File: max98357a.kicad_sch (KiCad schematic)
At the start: 12 parts, among them U6 MAX98357A

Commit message: ESP32S3 push before GPIO label changes
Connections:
- net pad renamed PAD
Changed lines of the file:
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@@
 		)
 	)
-	(hierarchical_label "pad"
+	(hierarchical_label "PAD"
 		(shape input)
 		(at 147.32 116.84 270)

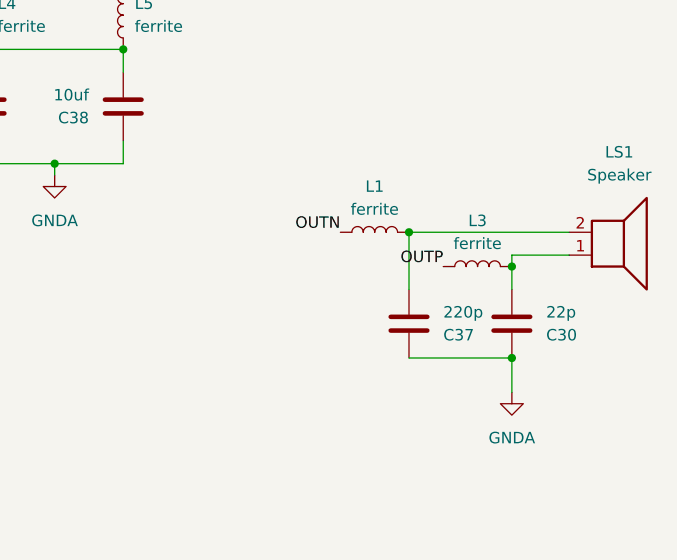
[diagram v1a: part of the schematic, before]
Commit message: ESP32S3: rename hierarchical GPIO labels and remove PCB tracks
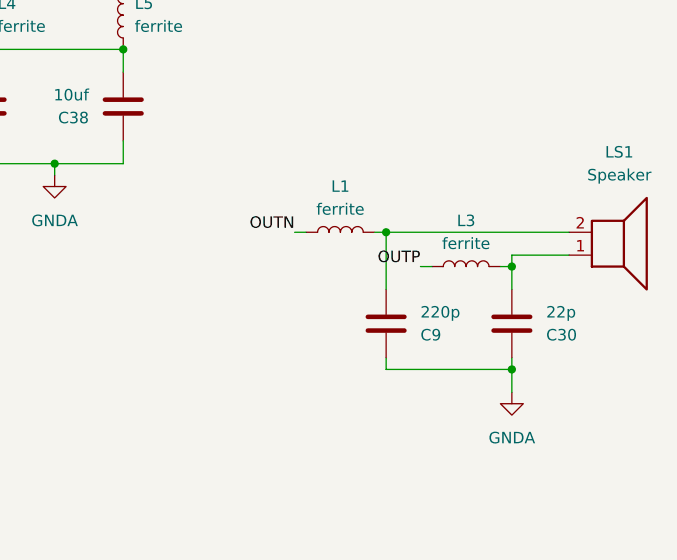
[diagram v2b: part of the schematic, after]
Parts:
- LS1: footprint (none) -> Connector_Molex:Molex_Micro-Latch_53253-0270_1x02_P2.00mm_Vertical
- renumbered C37 to C9
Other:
- moved on the sheet: C9, L1, L3
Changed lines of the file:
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@@
 	)
 	(junction
-		(at 220.98 106.68)
+		(at 232.41 110.49)
 		(diameter 0)
 		(color 0 0 0 0)
 	)
 	(junction
-		(at 232.41 120.65)
+		(at 218.44 106.68)
 		(diameter 0)
 		(color 0 0 0 0)
@@
 	)
 	(junction
-		(at 232.41 110.49)
+		(at 232.41 121.92)
 		(diameter 0)
 		(color 0 0 0 0)
@@
 	(wire
 		(pts
-			(xy 232.41 120.65) (xy 220.98 120.65)
+			(xy 232.41 121.92) (xy 218.44 121.92)
+		)
+		(stroke
+			(width 0)
+			(type default)
+		)
+	)
+	(wire
+		(pts
+			(xy 218.44 106.68) (xy 218.44 113.03)
 		)
 		(stroke
@@
 	(wire
 		(pts
-			(xy 220.98 106.68) (xy 220.98 113.03)
-		)
-		(stroke
-			(width 0)
-			(type default)
-		)
-	)
-	(wire
-		(pts
 			(xy 173.99 96.52) (xy 173.99 99.06)
 		)
@@
 	(wire
 		(pts
+			(xy 208.28 106.68) (xy 209.55 106.68)
+		)
+		(stroke
+			(width 0)
+			(type default)
+		)
+	)
+	(wire
+		(pts
 			(xy 173.99 86.36) (xy 189.23 86.36)
 		)
@@
 	(wire
 		(pts
+			(xy 231.14 110.49) (xy 232.41 110.49)
+		)
+		(stroke
+			(width 0)
+			(type default)
+		)
+	)
+	(wire
+		(pts
 			(xy 173.99 99.06) (xy 181.61 99.06)
 		)
@@
 	(wire
 		(pts
+			(xy 218.44 106.68) (xy 238.76 106.68)
+		)
+		(stroke
+			(width 0)
+			(type default)
+		)
+	)
+	(wire
+		(pts
 			(xy 121.92 120.65) (xy 121.92 116.84)
 		)
@@
 	(wire
 		(pts
+			(xy 232.41 121.92) (xy 232.41 124.46)
+		)
+		(stroke
+			(width 0)
+			(type default)
+		)
+	)
+	(wire
+		(pts
 			(xy 189.23 99.06) (xy 181.61 99.06)
 		)
@@
 	(wire
 		(pts
+			(xy 218.44 121.92) (xy 218.44 120.65)
+		)
+		(stroke
+			(width 0)
+			(type default)
+		)
+	)
+	(wire
+		(pts
 			(xy 83.82 139.7) (xy 74.93 139.7)
 		)
@@
 	(wire
 		(pts
-			(xy 238.76 106.68) (xy 220.98 106.68)
+			(xy 222.25 110.49) (xy 223.52 110.49)
 		)
 		(stroke
@@
 	(wire
 		(pts
+			(xy 232.41 121.92) (xy 232.41 120.65)
+		)
+		(stroke
+			(width 0)
+			(type default)
+		)
+	)
+	(wire
+		(pts
 			(xy 189.23 88.9) (xy 189.23 86.36)
 		)
@@
 	(wire
 		(pts
-			(xy 232.41 120.65) (xy 232.41 124.46)
-		)
-		(stroke
-			(width 0)
-			(type default)
-		)
-	)
-	(wire
-		(pts
 			(xy 118.11 101.6) (xy 132.08 101.6)
+		)
+		(stroke
+			(width 0)
+			(type default)
+		)
+	)
+	(wire
+		(pts
+			(xy 217.17 106.68) (xy 218.44 106.68)
 		)
 		(stroke
@@
 	)
 	(label "OUTP"
-		(at 224.79 110.49 180)
+		(at 222.25 110.49 180)
 		(effects
 			(font
@@
 	)
 	(label "OUTN"
-		(at 213.36 106.68 180)
+		(at 208.28 106.68 180)
 		(effects
 			(font
@@
 			)
 		)
-		(property "Footprint" ""
+		(property "Footprint" "Connector_Molex:Molex_Micro-Latch_53253-0270_1x02_P2.00mm_Vertical"
 			(at 243.84 104.14 0)
 			(hide yes)
@@
 	(symbol
 		(lib_id "Device:C")
-		(at 220.98 116.84 0)
+		(at 218.44 116.84 0)
 		(mirror x)
 		(unit 1)
@@
 		(in_pos_files yes)
 		(dnp no)
-		(property "Reference" "C37"
-			(at 224.79 118.11 0)
+		(property "Reference" "C9"
+			(at 222.25 118.11 0)
 			(show_name no)
 			(do_not_autoplace no)
@@
 		)
 		(property "Value" "220p"
-			(at 224.79 115.57 0)
+			(at 222.25 115.57 0)
 			(show_name no)
 			(do_not_autoplace no)
@@
 		)
 		(property "Footprint" "Capacitor_SMD:C_0805_2012Metric"
-			(at 221.9452 113.03 0)
+			(at 219.4052 113.03 0)
 			(hide yes)
 			(show_name no)
@@
 		)
 		(property "Datasheet" ""
-			(at 220.98 116.84 0)
+			(at 218.44 116.84 0)
 			(hide yes)
 			(show_name no)
@@
 		)
 		(property "Description" ""
-			(at 220.98 116.84 0)
+			(at 218.44 116.84 0)
 			(show_name no)
 			(do_not_autoplace no)
@@
 			(project "esp32_xiaozhi"
 				(path "/cae338e8-f342-43cb-b99a-a0486629133c/0b8c63fc-3109-4f1a-8140-b91a685f434f"
-					(reference "C37")
+					(reference "C9")
 					(unit 1)
 				)
@@
 	(symbol
 		(lib_id "Device:L")
-		(at 217.17 106.68 90)
+		(at 213.36 106.68 90)
 		(unit 1)
 		(body_style 1)
@@
 		(fields_autoplaced yes)
 		(property "Reference" "L1"
-			(at 217.17 101.6 90)
+			(at 213.36 101.6 90)
 			(show_name no)
 			(do_not_autoplace no)
@@
 		)
 		(property "Value" "ferrite"
-			(at 217.17 104.14 90)
+			(at 213.36 104.14 90)
 			(show_name no)
 			(do_not_autoplace no)
@@
 		)
 		(property "Footprint" ""
-			(at 217.17 106.68 0)
+			(at 213.36 106.68 0)
 			(hide yes)
 			(show_name no)
@@
 		)
 		(property "Datasheet" ""
-			(at 217.17 106.68 0)
+			(at 213.36 106.68 0)
 			(hide yes)
 			(show_name no)
@@
 		)
 		(property "Description" "Inductor"
-			(at 217.17 106.68 0)
+			(at 213.36 106.68 0)
 			(hide yes)
 			(show_name no)
@@
 	(symbol
 		(lib_id "Device:L")
-		(at 228.6 110.49 90)
+		(at 227.33 110.49 90)
 		(unit 1)
 		(body_style 1)
@@
 		(fields_autoplaced yes)
 		(property "Reference" "L3"
-			(at 228.6 105.41 90)
+			(at 227.33 105.41 90)
 			(show_name no)
 			(do_not_autoplace no)
@@
 		)
 		(property "Value" "ferrite"
-			(at 228.6 107.95 90)
+			(at 227.33 107.95 90)
 			(show_name no)
 			(do_not_autoplace no)
@@
 		)
 		(property "Footprint" ""
-			(at 228.6 110.49 0)
+			(at 227.33 110.49 0)
 			(hide yes)
 			(show_name no)
@@
 		)
 		(property "Datasheet" ""
-			(at 228.6 110.49 0)
+			(at 227.33 110.49 0)
 			(hide yes)
 			(show_name no)
@@
 		)
 		(property "Description" "Inductor"
-			(at 228.6 110.49 0)
-			(hide yes)
-			(show_name no)
+			(at 227.33 110.49 0)
+			(hide yes)
+			(show_name no)

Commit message: Actualización de esquemáticos y PCB
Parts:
- added J7: Conn_01x07_Pin, Connector_PinHeader_2.54mm:PinHeader_1x07_P2.54mm_Vertical, symbol Connector:Conn_01x07_Pin
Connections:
- net BCLK: now also J7.5 (Pin_5)
- net DIN: now also J7.6 (Pin_6)
- net GAIN: now also J7.1 (Pin_1)
- net GNDA: now also J7.7 (Pin_7)
- net LRC: now also J7.4 (Pin_4)
- net SD: now also J7.2 (Pin_2)
- net at C28.2, C38.2, L4.1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: now also J7.3 (Pin_3)
